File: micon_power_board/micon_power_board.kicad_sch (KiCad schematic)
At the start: 18 parts, among them J1 Conn_01x02_Pin, J2 Conn_01x02_Pin, J3 Conn_01x02_Pin, J4 Conn_01x02_Pin, J5 Conn_01x02_Pin, J6 Conn_01x02_Pin, J7 Conn_01x02_Socket, U1 M78AR05-1

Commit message: マイコン電源基板　基板完成 ver0.1
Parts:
- D1: Buy_URL (none) -> https://akizukidenshi.com/catalog/g/g116378/
- J6: Buy_URL (none) -> https://akizukidenshi.com/catalog/g/g117949/
- J7: Buy_URL (none) -> https://akizukidenshi.com/catalog/g/g117948/
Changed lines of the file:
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@@
 			)
 		)
-		(property "Description" "Generic connector, single row, 01x02, script generated"
+		(property "Description" "DF1E-2P-2.5DS"
 			(at 95.25 17.78 0)
 			(hide yes)
@@
 			)
 		)
-		(property "Description" "Unpolarized capacitor"
+		(property "Description" "2.2μF100V X7S"
 			(at 104.14 54.61 0)
 			(hide yes)
@@
 			)
 		)
-		(property "Description" "Generic connector, single row, 01x02, script generated"
+		(property "Description" "DF1E-2P-2.5DS"
 			(at 60.96 17.78 0)
 			(hide yes)
@@
 			)
 		)
-		(property "Description" "Generic connector, single row, 01x02, script generated"
+		(property "Description" "DF1E-2P-2.5DS"
 			(at 72.39 17.78 0)
 			(hide yes)
@@
 			)
 		)
-		(property "Description" "Generic connector, single row, 01x02, script generated"
+		(property "Description" "DF1E-2P-2.5DS"
 			(at 83.82 17.78 0)
 			(hide yes)
@@
 			)
 		)
-		(property "Description" "Generic connector, single row, 01x02, script generated"
+		(property "Description" "XT30PW-F"
+			(at 34.29 29.21 0)
+			(hide yes)
+			(show_name no)
+			(do_not_autoplace no)
+			(effects
+				(font
+					(size 1.27 1.27)
+				)
+			)
+		)
+		(property "Buy_URL" "https://akizukidenshi.com/catalog/g/g117948/"
 			(at 34.29 29.21 0)
 			(hide yes)
@@
 			)
 		)
+		(property "Buy_URL" "https://akizukidenshi.com/catalog/g/g116378/"
+			(at 43.18 49.53 0)
+			(hide yes)
+			(show_name no)
+			(do_not_autoplace no)
+			(effects
+				(font
+					(size 1.27 1.27)
+				)
+			)
+		)
 		(pin "1"
 		)
@@
 			)
 		)
-		(property "Description" "Generic connector, single row, 01x02, script generated"
+		(property "Description" "DF1E-2P-2.5DS"
 			(at 106.68 17.78 0)
 			(hide yes)
@@
 			)
 		)
-		(property "Description" "Generic connector, single row, 01x02, script generated"
+		(property "Description" "XT30PW-M"
+			(at 22.86 29.21 0)
+			(hide yes)
+			(show_name no)
+			(do_not_autoplace no)
+			(effects
+				(font
+					(size 1.27 1.27)
+				)
+			)
+		)
+		(property "Buy_URL" "https://akizukidenshi.com/catalog/g/g117949/"
 			(at 22.86 29.21 0)
 			(hide yes)
@@
 			)
 		)
-		(property "Description" "Unpolarized capacitor"
+		(property "Description" "2.2μF100V X7S"
 			(at 96.52 54.61 0)
 			(hide yes)

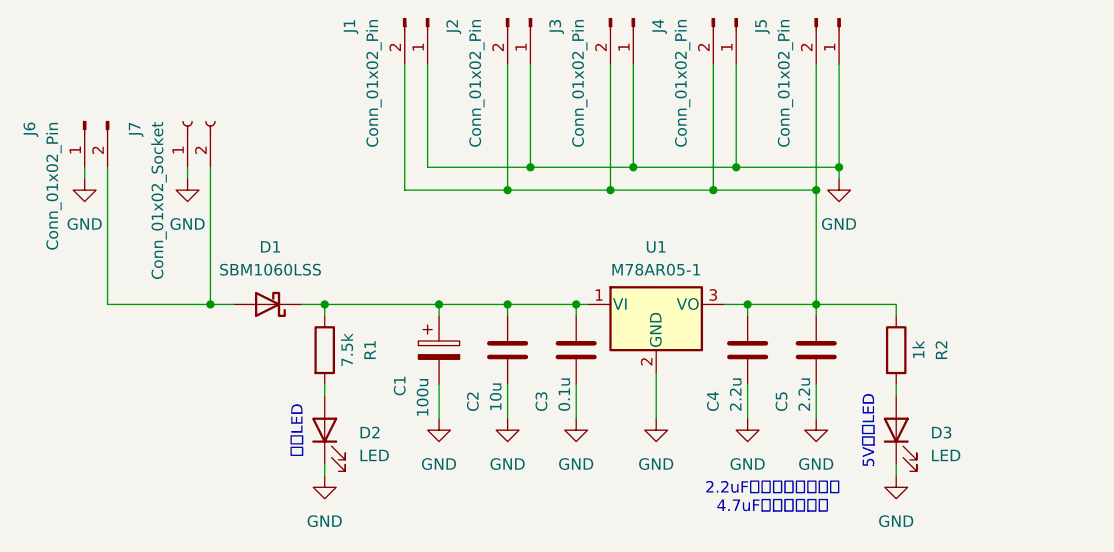
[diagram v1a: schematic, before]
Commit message: マイコン電源基板　基板にテストポイントを追加，ver 0.5
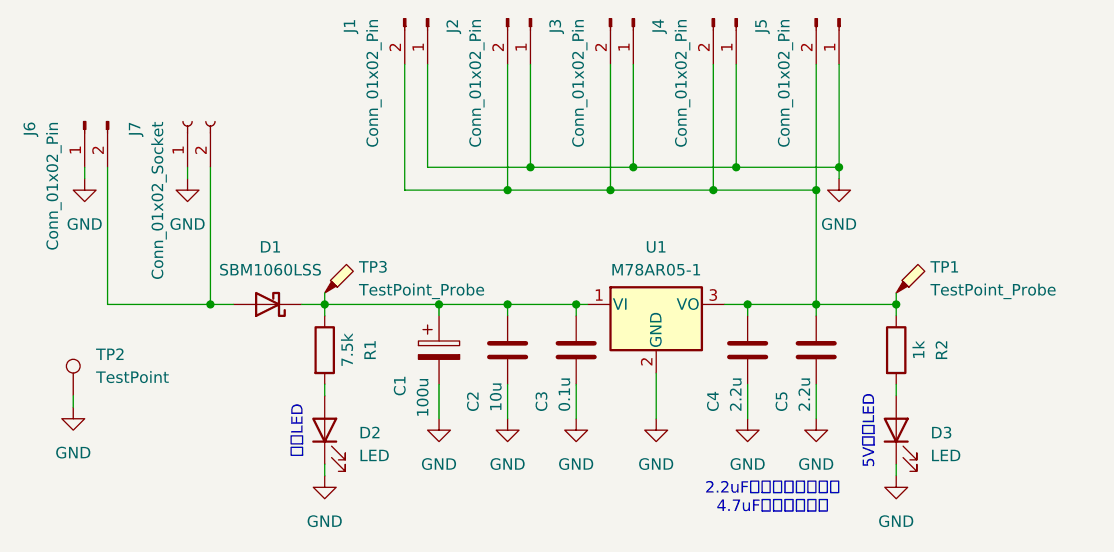
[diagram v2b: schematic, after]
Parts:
- added TP1, TP3: TestPoint_Probe, TestPoint:TestPoint_THTPad_D2.0mm_Drill1.0mm, symbol Connector:TestPoint_Probe
- added TP2: TestPoint, TestPoint:TestPoint_THTPad_D2.0mm_Drill1.0mm, symbol Connector:TestPoint
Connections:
- net GND: now also TP2.1
- net at C4.1, C5.1, J1.2 (Pin_2)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: now also TP1.1
- net at C1.1, C2.1, C3.1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: now also TP3.1

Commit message: マイコン電源基板　0.1uFのコンデンサの耐圧を他と揃えるため，変更，ver 0.7
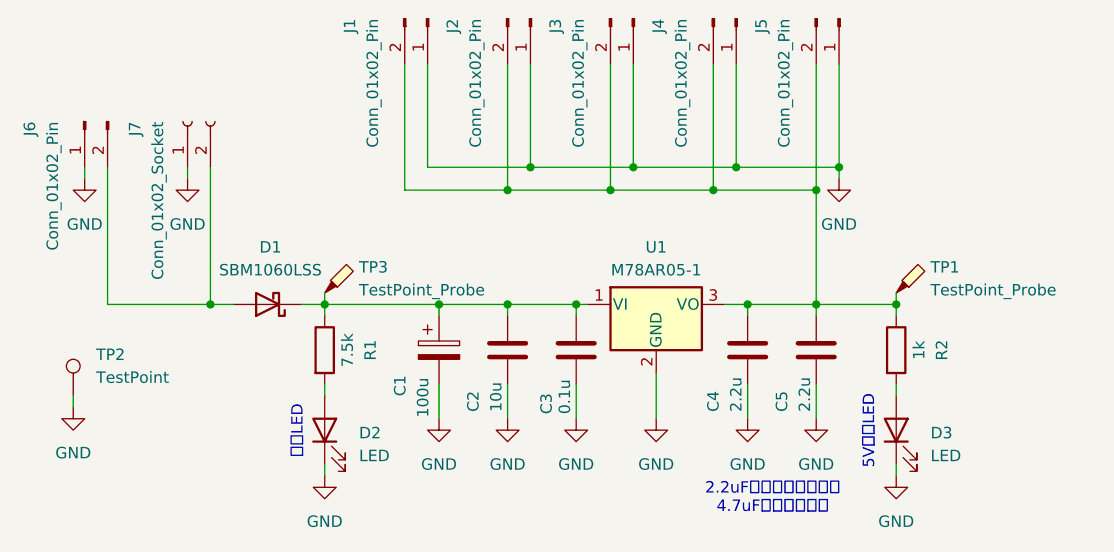
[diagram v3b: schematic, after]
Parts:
- C3: footprint Capacitor_THT:C_Disc_D4.7mm_W2.5mm_P5.00mm -> Capacitor_THT:C_Disc_D5.0mm_W2.5mm_P2.50mm; Buy_URL https://akizukidenshi.com/catalog/g/g115927/ -> https://akizukidenshi.com/catalog/g/g113582/
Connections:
- net GND: now also C3.1; no longer C3.2
- net at C1.1, C2.1, D1.1 (K)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: now also C3.2; no longer C3.1
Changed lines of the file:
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@@
+	)
+	(symbol
+		(lib_id "Device:C")
+		(at 77.47 54.61 0)
+		(mirror x)
+		(unit 1)
+		(body_style 1)
+		(exclude_from_sim no)
+		(in_bom yes)
+		(on_board yes)
+		(in_pos_files yes)
+		(dnp no)
+		(property "Reference" "C3"
+			(at 74.168 61.722 90)
+			(show_name no)
+			(do_not_autoplace no)
+			(effects
+				(font
+					(size 1.27 1.27)
+				)
+				(justify right)
+			)
+		)
+		(property "Value" "0.1u"
+			(at 76.2 61.722 90)
+			(show_name no)
+			(do_not_autoplace no)
+			(effects
+				(font
+					(size 1.27 1.27)
+				)
+				(justify right)
+			)
+		)
+		(property "Footprint" "Capacitor_THT:C_Disc_D5.0mm_W2.5mm_P2.50mm"
+			(at 78.4352 50.8 0)
+			(hide yes)
+			(show_name no)
+			(do_not_autoplace no)
+			(effects
+				(font
+					(size 1.27 1.27)
+				)
+			)
+		)
+		(property "Datasheet" ""
+			(at 77.47 54.61 0)
+			(hide yes)
+			(show_name no)
+			(do_not_autoplace no)
+			(effects
+				(font
+					(size 1.27 1.27)
+				)
+			)
+		)
+		(property "Description" "0.1μF50V X7R"
+			(at 77.47 54.61 0)
+			(hide yes)
+			(show_name no)
+			(do_not_autoplace no)
+			(effects
+				(font
+					(size 1.27 1.27)
+				)
+			)
+		)
+		(property "Buy_URL" "https://akizukidenshi.com/catalog/g/g113582/"
+			(at 77.47 54.61 0)
+			(hide yes)
+			(show_name no)
+			(do_not_autoplace no)
+			(effects
+				(font
+					(size 1.27 1.27)
+				)
+			)
+		)
+		(pin "2"
+		)
+		(pin "1"
+		)
+		(instances
+			(project "micon_power_board"
+				(path "/ffb185b6-b8aa-4975-b056-1915a949a353"
+					(reference "C3")
+					(unit 1)
+				)
+			)
+		)
 	)
 	(symbol
@@
 					(unit 1)
 				)
-			)
-		)
-	)
-	(symbol
-		(lib_id "Device:C")
-		(at 77.47 54.61 0)
-		(unit 1)
-		(body_style 1)
-		(exclude_from_sim no)
-		(in_bom yes)
-		(on_board yes)
-		(in_pos_files yes)
-		(dnp no)
-		(property "Reference" "C3"
-			(at 73.66 61.468 90)
-			(show_name no)
-			(do_not_autoplace no)
-			(effects
-				(font
-					(size 1.27 1.27)
-				)
-				(justify left)
-			)
-		)
-		(property "Value" "0.1u"
-			(at 76.2 61.468 90)
-			(show_name no)
-			(do_not_autoplace no)
-			(effects
-				(font
-					(size 1.27 1.27)
-				)
-				(justify left)
-			)
-		)
-		(property "Footprint" "Capacitor_THT:C_Disc_D4.7mm_W2.5mm_P5.00mm"
-			(at 78.4352 58.42 0)
-			(hide yes)
-			(show_name no)
-			(do_not_autoplace no)
-			(effects
-				(font
-					(size 1.27 1.27)
-				)
-			)
-		)
-		(property "Datasheet" ""
-			(at 77.47 54.61 0)
-			(hide yes)
-			(show_name no)
-			(do_not_autoplace no)
-			(effects
-				(font
-					(size 1.27 1.27)
-				)
-			)
-		)
-		(property "Description" "0.1μF100V X7R"
-			(at 77.47 54.61 0)
-			(hide yes)
-			(show_name no)
-			(do_not_autoplace no)
-			(effects
-				(font
-					(size 1.27 1.27)
-				)
-			)
-		)
-		(property "Buy_URL" "https://akizukidenshi.com/catalog/g/g115927/"
-			(at 77.47 54.61 90)
-			(hide yes)
-			(show_name no)
-			(do_not_autoplace no)
-			(effects
-				(font
-					(size 1.27 1.27)
-				)
-			)
-		)
-		(pin "1"
-		)
-		(pin "2"
-		)
-		(instances
-			(project "micon_power_board"
-				(path "/ffb185b6-b8aa-4975-b056-1915a949a353"
-					(reference "C3")
-					(unit 1)
-				)

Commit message: マイコン電源基板　シルクを一部修正，ver 1.0
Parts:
- renumbered TP3 to TP1, TP1 to TP2, TP2 to TP3
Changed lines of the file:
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@@
 		(dnp no)
 		(fields_autoplaced yes)
-		(property "Reference" "TP2"
+		(property "Reference" "TP3"
 			(at 24.13 55.1179 0)
 			(show_name no)
@@
 			(project "micon_power_board"
 				(path "/ffb185b6-b8aa-4975-b056-1915a949a353"
-					(reference "TP2")
+					(reference "TP3")
 					(unit 1)
 				)
@@
 		(dnp no)
 		(fields_autoplaced yes)
-		(property "Reference" "#PWR012"
+		(property "Reference" "#PWR04"
 			(at 21.59 67.31 0)
 			(hide yes)
@@
 			(project "micon_power_board"
 				(path "/ffb185b6-b8aa-4975-b056-1915a949a353"
-					(reference "#PWR012")
+					(reference "#PWR04")
 					(unit 1)
 				)
@@
 		(dnp no)
 		(fields_autoplaced yes)
-		(property "Reference" "#PWR09"
+		(property "Reference" "#PWR010"
 			(at 104.14 68.58 0)
 			(hide yes)
@@
 			(project "micon_power_board"
 				(path "/ffb185b6-b8aa-4975-b056-1915a949a353"
-					(reference "#PWR09")
+					(reference "#PWR010")
 					(unit 1)
 				)
@@
 		(dnp no)
 		(fields_autoplaced yes)
-		(property "Reference" "TP3"
+		(property "Reference" "TP1"
 			(at 53.34 45.4024 0)
 			(show_name no)
@@
 			(project "micon_power_board"
 				(path "/ffb185b6-b8aa-4975-b056-1915a949a353"
-					(reference "TP3")
+					(reference "TP1")
 					(unit 1)
 				)
@@
 		(dnp no)
 		(fields_autoplaced yes)
-		(property "Reference" "#PWR011"
+		(property "Reference" "#PWR012"
 			(at 113.03 74.93 0)
 			(hide yes)
@@
 			(project "micon_power_board"
 				(path "/ffb185b6-b8aa-4975-b056-1915a949a353"
-					(reference "#PWR011")
+					(reference "#PWR012")
 					(unit 1)
 				)
@@
 		(dnp no)
 		(fields_autoplaced yes)
-		(property "Reference" "#PWR07"
+		(property "Reference" "#PWR08"
 			(at 86.36 68.58 0)
 			(hide yes)
@@
 			(project "micon_power_board"
 				(path "/ffb185b6-b8aa-4975-b056-1915a949a353"
-					(reference "#PWR07")
+					(reference "#PWR08")
 					(unit 1)
 				)
@@
 		(dnp no)
 		(fields_autoplaced yes)
-		(property "Reference" "#PWR06"
+		(property "Reference" "#PWR07"
 			(at 77.47 68.58 0)
 			(hide yes)
@@
 			(project "micon_power_board"
 				(path "/ffb185b6-b8aa-4975-b056-1915a949a353"
-					(reference "#PWR06")
+					(reference "#PWR07")
 					(unit 1)
 				)
@@
 		(dnp no)
 		(fields_autoplaced yes)
-		(property "Reference" "#PWR08"
+		(property "Reference" "#PWR09"
 			(at 96.52 68.58 0)
 			(hide yes)
@@
 			(project "micon_power_board"
 				(path "/ffb185b6-b8aa-4975-b056-1915a949a353"
-					(reference "#PWR08")
+					(reference "#PWR09")
 					(unit 1)
 				)
@@
 		(dnp no)
 		(fields_autoplaced yes)
-		(property "Reference" "#PWR04"
+		(property "Reference" "#PWR05"
 			(at 62.23 68.58 0)
 			(hide yes)
@@
 			(project "micon_power_board"
 				(path "/ffb185b6-b8aa-4975-b056-1915a949a353"
-					(reference "#PWR04")
+					(reference "#PWR05")
 					(unit 1)
 				)
@@
 		(dnp no)
 		(fields_autoplaced yes)
-		(property "Reference" "#PWR05"
+		(property "Reference" "#PWR06"
 			(at 69.85 68.58 0)
 			(hide yes)
@@
 			(project "micon_power_board"
 				(path "/ffb185b6-b8aa-4975-b056-1915a949a353"
-					(reference "#PWR05")
+					(reference "#PWR06")
 					(unit 1)
 				)
@@
 		(dnp no)
 		(fields_autoplaced yes)
-		(property "Reference" "#PWR010"
+		(property "Reference" "#PWR011"
 			(at 49.53 74.93 0)
 			(hide yes)
@@
 			(project "micon_power_board"
 				(path "/ffb185b6-b8aa-4975-b056-1915a949a353"
-					(reference "#PWR010")
+					(reference "#PWR011")
 					(unit 1)
 				)
@@
 		(dnp no)
 		(fields_autoplaced yes)
-		(property "Reference" "TP1"
+		(property "Reference" "TP2"
 			(at 116.84 45.4024 0)
 			(show_name no)
@@
 			(project "micon_power_board"
 				(path "/ffb185b6-b8aa-4975-b056-1915a949a353"
-					(reference "TP1")
-					(unit 1)
-				)
+					(reference "TP2")
+					(unit 1)
+				)
